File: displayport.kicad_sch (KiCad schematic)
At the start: 56 parts

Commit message: add UART4 connector
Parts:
- C191: renamed from C189; value (none) -> 0.1uF; footprint (none) -> Capacitor_SMD:C_0402_1005Metric
- C194: renamed from C192; value (none) -> 1uF; footprint (none) -> Capacitor_SMD:C_0402_1005Metric
- C200: renamed from C198; value (none) -> 1uF; footprint (none) -> Capacitor_SMD:C_0402_1005Metric
- C206: renamed from C204; value (none) -> 0.1uF; footprint (none) -> qsbc:C_0201_0603Metric
- C207: renamed from C205; value (none) -> 0.1uF; footprint (none) -> qsbc:C_0201_0603Metric
- C208: renamed from C206; value (none) -> 0.1uF; footprint (none) -> qsbc:C_0201_0603Metric
- C209: renamed from C207; value (none) -> 0.1uF; footprint (none) -> qsbc:C_0201_0603Metric
- C210: renamed from C208; value (none) -> 0.1uF; footprint (none) -> qsbc:C_0201_0603Metric
- C211: renamed from C209; value (none) -> 0.1uF; footprint (none) -> qsbc:C_0201_0603Metric
- C212: renamed from C210; value (none) -> 0.1uF; footprint (none) -> qsbc:C_0201_0603Metric
- C213: renamed from C211; value (none) -> 0.1uF; footprint (none) -> qsbc:C_0201_0603Metric
- C214: renamed from C212; value (none) -> 0.1uF; footprint (none) -> qsbc:C_0201_0603Metric
- C215: renamed from C213; value (none) -> 0.1uF; footprint (none) -> qsbc:C_0201_0603Metric
- C218: renamed from C216; value (none) -> 1000pF; footprint (none) -> Capacitor_SMD:C_1210_3225Metric
- R140: renamed from R141; value (none) -> 10K; footprint (none) -> Resistor_SMD:R_0402_1005Metric
- R141: renamed from R142; value (none) -> R; footprint (none) -> Resistor_SMD:R_0402_1005Metric
- R142: renamed from R143; value (none) -> R; footprint (none) -> Resistor_SMD:R_0402_1005Metric
- R145: renamed from R146; value (none) -> 100K; footprint (none) -> Resistor_SMD:R_0402_1005Metric
- R146: renamed from R147; value (none) -> 100K; footprint (none) -> Resistor_SMD:R_0402_1005Metric
- R148: renamed from R149; value (none) -> 1M; footprint (none) -> Resistor_SMD:R_0402_1005Metric
- R150: renamed from R151; value (none) -> 1M; footprint (none) -> Resistor_SMD:R_1206_3216Metric
- U1: value (none) -> MIMX8MM6DVTLZAA; footprint (none) -> qsbc:SOT1967-1
- U35: renamed from U34; value (none) -> LP5912-1.2DRV; footprint (none) -> Package_SON:WSON-6-1EP_2x2mm_P0.65mm_EP1x1.6mm_ThermalVias
- U36: renamed from U35; value (none) -> SN65DSI86; footprint (none) -> qsbc:BGA-64
- U37: renamed from U36; value (none) -> TPD4E02B04; footprint (none) -> Package_SON:USON-10_2.5x1.0mm_P0.5mm
- U38: renamed from U37; value (none) -> TPD4E02B04; footprint (none) -> Package_SON:USON-10_2.5x1.0mm_P0.5mm
- U39: renamed from U38; value (none) -> TPD4E02B04; footprint (none) -> Package_SON:USON-10_2.5x1.0mm_P0.5mm
- U40: renamed from U39; value (none) -> Connector_Displayport_Source; footprint (none) -> qsbc:Connector_Displayport_Molex_472720001
- X1: value (none) -> 26Mhz; footprint (none) -> Oscillator:Oscillator_SMD_ECS_2520MV-xxx-xx-4Pin_2.5x2.0mm
- renumbered C185 to C187, C186 to C188, C187 to C189, C188 to C190, C190 to C192, C191 to C193, C193 to C195, C194 to C196, C195 to C197, C196 to C198, C197 to C199, C199 to C201, C200 to C202, C201 to C203, C202 to C204, C203 to C205, C214 to C216, C215 to C217, R136 to R135, R137 to R136, R138 to R137, R139 to R138, R140 to R139, R144 to R143, R145 to R144, R148 to R147, R150 to R149

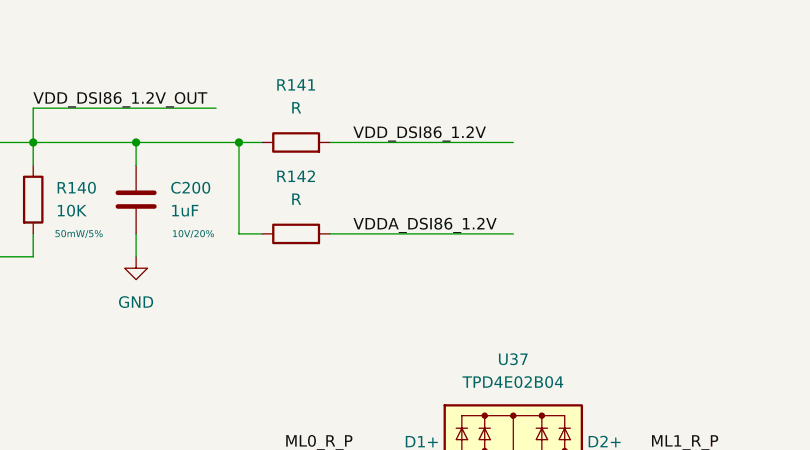
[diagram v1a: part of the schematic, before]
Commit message: change USB-UART conn, add new 0402 fp, more pcb work
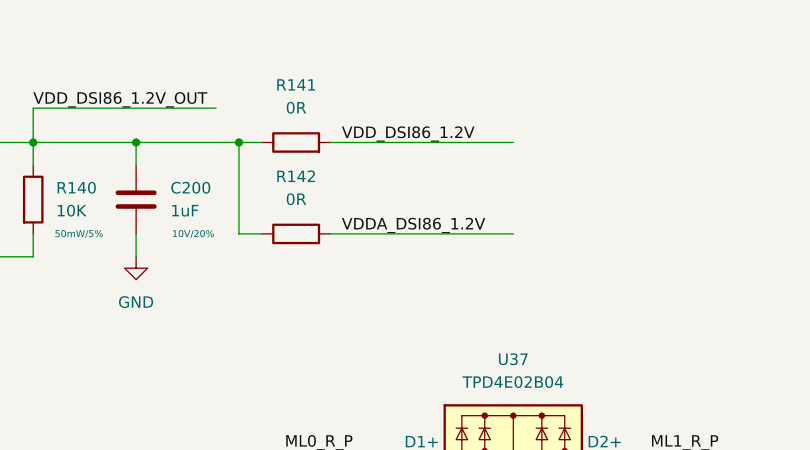
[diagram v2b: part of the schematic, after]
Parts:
- C190, C191, C194, C195, C200, C203: footprint Capacitor_SMD:C_0402_1005Metric -> qsbc:C_0402_1005Metric
- R135, R136, R137, R138, R139, R140, R143, R144, R145, R146, R147, R148, R149: footprint Resistor_SMD:R_0402_1005Metric -> qsbc:R_0402_1005Metric
- R141, R142: value R -> 0R; footprint Resistor_SMD:R_0402_1005Metric -> qsbc:R_0402_1005Metric
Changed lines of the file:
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@@
     (effects (font (size 1.27 1.27)) (justify left bottom))
   )
-  (label "VDDA_DSI86_1.2V" (at 228.6 40.64 0)
+  (label "VDDA_DSI86_1.2V" (at 227.33 40.64 0)
     (effects (font (size 1.27 1.27)) (justify left bottom))
   )
@@
     (effects (font (size 1.27 1.27)) (justify left bottom))
   )
-  (label "VDD_DSI86_1.2V" (at 228.6 30.48 0)
+  (label "VDD_DSI86_1.2V" (at 227.33 30.48 0)
     (effects (font (size 1.27 1.27)) (justify left bottom))
   )
@@
       (effects (font (size 1.27 1.27)) (justify left))
     )
-    (property "Footprint" "Resistor_SMD:R_0402_1005Metric" (id 2) (at 326.898 130.81 90)
+    (property "Footprint" "qsbc:R_0402_1005Metric" (id 2) (at 326.898 130.81 90)
       (effects (font (size 1.27 1.27)) hide)
     )
@@
       (effects (font (size 1.27 1.27)) (justify left))
     )
-    (property "Footprint" "Capacitor_SMD:C_0402_1005Metric" (id 2) (at 242.2652 246.38 0)
+    (property "Footprint" "qsbc:C_0402_1005Metric" (id 2) (at 242.2652 246.38 0)
       (effects (font (size 1.27 1.27)) hide)
     )
@@
     (property "Reference" "R144" (id 0) (at 238.76 147.32 90))
     (property "Value" "51K" (id 1) (at 238.76 149.86 90))
-    (property "Footprint" "Resistor_SMD:R_0402_1005Metric" (id 2) (at 238.76 155.448 90)
+    (property "Footprint" "qsbc:R_0402_1005Metric" (id 2) (at 238.76 155.448 90)
       (effects (font (size 1.27 1.27)) hide)
     )
@@
       (effects (font (size 1.27 1.27)) (justify left))
     )
-    (property "Footprint" "Capacitor_SMD:C_0402_1005Metric" (id 2) (at 205.4352 40.64 0)
+    (property "Footprint" "qsbc:C_0402_1005Metric" (id 2) (at 205.4352 40.64 0)
       (effects (font (size 1.27 1.27)) hide)
     )
@@
       (effects (font (size 1.27 1.27)) (justify left))
     )
-    (property "Footprint" "Resistor_SMD:R_0402_1005Metric" (id 2) (at 115.062 102.87 90)
+    (property "Footprint" "qsbc:R_0402_1005Metric" (id 2) (at 115.062 102.87 90)
       (effects (font (size 1.27 1.27)) hide)
     )
@@
     (property "Reference" "R149" (id 0) (at 359.41 100.33 90))
     (property "Value" "0R" (id 1) (at 359.41 102.87 90))
-    (property "Footprint" "Resistor_SMD:R_0402_1005Metric" (id 2) (at 359.41 108.458 90)
+    (property "Footprint" "qsbc:R_0402_1005Metric" (id 2) (at 359.41 108.458 90)
       (effects (font (size 1.27 1.27)) hide)
     )
@@
       (effects (font (size 1.27 1.27)) (justify left))
     )
-    (property "Footprint" "Resistor_SMD:R_0402_1005Metric" (id 2) (at 347.218 130.81 90)
+    (property "Footprint" "qsbc:R_0402_1005Metric" (id 2) (at 347.218 130.81 90)
       (effects (font (size 1.27 1.27)) hide)
     )
@@
       (effects (font (size 1.27 1.27)) (justify left))
     )
-    (property "Footprint" "Resistor_SMD:R_0402_1005Metric" (id 2) (at 126.492 115.57 90)
+    (property "Footprint" "qsbc:R_0402_1005Metric" (id 2) (at 126.492 115.57 90)
       (effects (font (size 1.27 1.27)) hide)
     )
@@
       (effects (font (size 1.27 1.27)) (justify left))
     )
-    (property "Footprint" "Capacitor_SMD:C_0402_1005Metric" (id 2) (at 111.4552 39.37 0)
+    (property "Footprint" "qsbc:C_0402_1005Metric" (id 2) (at 111.4552 39.37 0)
       (effects (font (size 1.27 1.27)) hide)
     )
@@
     (in_bom yes) (on_board yes) (fields_autoplaced)
     (property "Reference" "R142" (id 0) (at 222.25 34.29 90))
-    (property "Value" "R" (id 1) (at 222.25 36.83 90))
-    (property "Footprint" "Resistor_SMD:R_0402_1005Metric" (id 2) (at 222.25 42.418 90)
+    (property "Value" "0R" (id 1) (at 222.25 36.83 90))
+    (property "Footprint" "qsbc:R_0402_1005Metric" (id 2) (at 222.25 42.418 90)
       (effects (font (size 1.27 1.27)) hide)
     )
@@
       (effects (font (size 1.27 1.27)) (justify left))
     )
-    (property "Footprint" "Resistor_SMD:R_0402_1005Metric" (id 2) (at 126.492 105.41 90)
+    (property "Footprint" "qsbc:R_0402_1005Metric" (id 2) (at 126.492 105.41 90)
       (effects (font (size 1.27 1.27)) hide)
     )
@@
       (effects (font (size 1.27 1.27)) (justify right))
     )
-    (property "Footprint" "Resistor_SMD:R_0402_1005Metric" (id 2) (at 333.502 130.81 90)
+    (property "Footprint" "qsbc:R_0402_1005Metric" (id 2) (at 333.502 130.81 90)
       (effects (font (size 1.27 1.27)) hide)
     )
@@
     (in_bom yes) (on_board yes) (fields_autoplaced)
     (property "Reference" "R141" (id 0) (at 222.25 24.13 90))
-    (property "Value" "R" (id 1) (at 222.25 26.67 90))
-    (property "Footprint" "Resistor_SMD:R_0402_1005Metric" (id 2) (at 222.25 32.258 90)
+    (property "Value" "0R" (id 1) (at 222.25 26.67 90))
+    (property "Footprint" "qsbc:R_0402_1005Metric" (id 2) (at 222.25 32.258 90)
       (effects (font (size 1.27 1.27)) hide)
     )
@@
       (effects (font (size 1.27 1.27)) (justify left))
     )
-    (property "Footprint" "Resistor_SMD:R_0402_1005Metric" (id 2) (at 115.062 92.71 90)
+    (property "Footprint" "qsbc:R_0402_1005Metric" (id 2) (at 115.062 92.71 90)
       (effects (font (size 1.27 1.27)) hide)
     )
@@
       (effects (font (size 1.27 1.27)) (justify left))
     )
-    (property "Footprint" "Resistor_SMD:R_0402_1005Metric" (id 2) (at 335.788 107.95 90)
+    (property "Footprint" "qsbc:R_0402_1005Metric" (id 2) (at 335.788 107.95 90)
       (effects (font (size 1.27 1.27)) hide)
     )
@@
       (effects (font (size 1.27 1.27)) (justify left))
     )
-    (property "Footprint" "Capacitor_SMD:C_0402_1005Metric" (id 2) (at 153.3652 246.38 0)
+    (property "Footprint" "qsbc:C_0402_1005Metric" (id 2) (at 153.3652 246.38 0)
       (effects (font (size 1.27 1.27)) hide)
     )
@@
     (property "Reference" "R139" (id 0) (at 142.24 78.74 90))
     (property "Value" "0R" (id 1) (at 142.24 81.28 90))
-    (property "Footprint" "Resistor_SMD:R_0402_1005Metric" (id 2) (at 142.24 85.598 90)
+    (property "Footprint" "qsbc:R_0402_1005Metric" (id 2) (at 142.24 85.598 90)
       (effects (font (size 1.27 1.27)) hide)
     )
@@
       (effects (font (size 1.27 1.27)) (justify left))
     )
-    (property "Footprint" "Capacitor_SMD:C_0402_1005Metric" (id 2) (at 152.0952 40.64 0)
+    (property "Footprint" "qsbc:C_0402_1005Metric" (id 2) (at 152.0952 40.64 0)
       (effects (font (size 1.27 1.27)) hide)
     )
@@
       (effects (font (size 1.27 1.27)) (justify left))
     )
-    (property "Footprint" "Resistor_SMD:R_0402_1005Metric" (id 2) (at 230.632 173.99 90)
+    (property "Footprint" "qsbc:R_0402_1005Metric" (id 2) (at 230.632 173.99 90)
       (effects (font (size 1.27 1.27)) hide)
     )
@@
       (effects (font (size 1.27 1.27)) (justify left))
     )
-    (property "Footprint" "Capacitor_SMD:C_0402_1005Metric" (id 2) (at 102.5652 246.38 0)
+    (property "Footprint" "qsbc:C_0402_1005Metric" (id 2) (at 102.5652 246.38 0)
       (effects (font (size 1.27 1.27)) hide)
     )
@@
       (effects (font (size 1.27 1.27)) (justify left))
     )
-    (property "Footprint" "Resistor_SMD:R_0402_1005Metric" (id 2) (at 191.262 36.83 90)
-      (effects (font (size 1.27 1.27)) hide)
-    )
+    (property "Footprint" "qsbc:R_0402_1005Metric" (id 2) (at 191.262 36.83 90)
+      (effects (font (size 1.27 1.27)) hide)
+    )

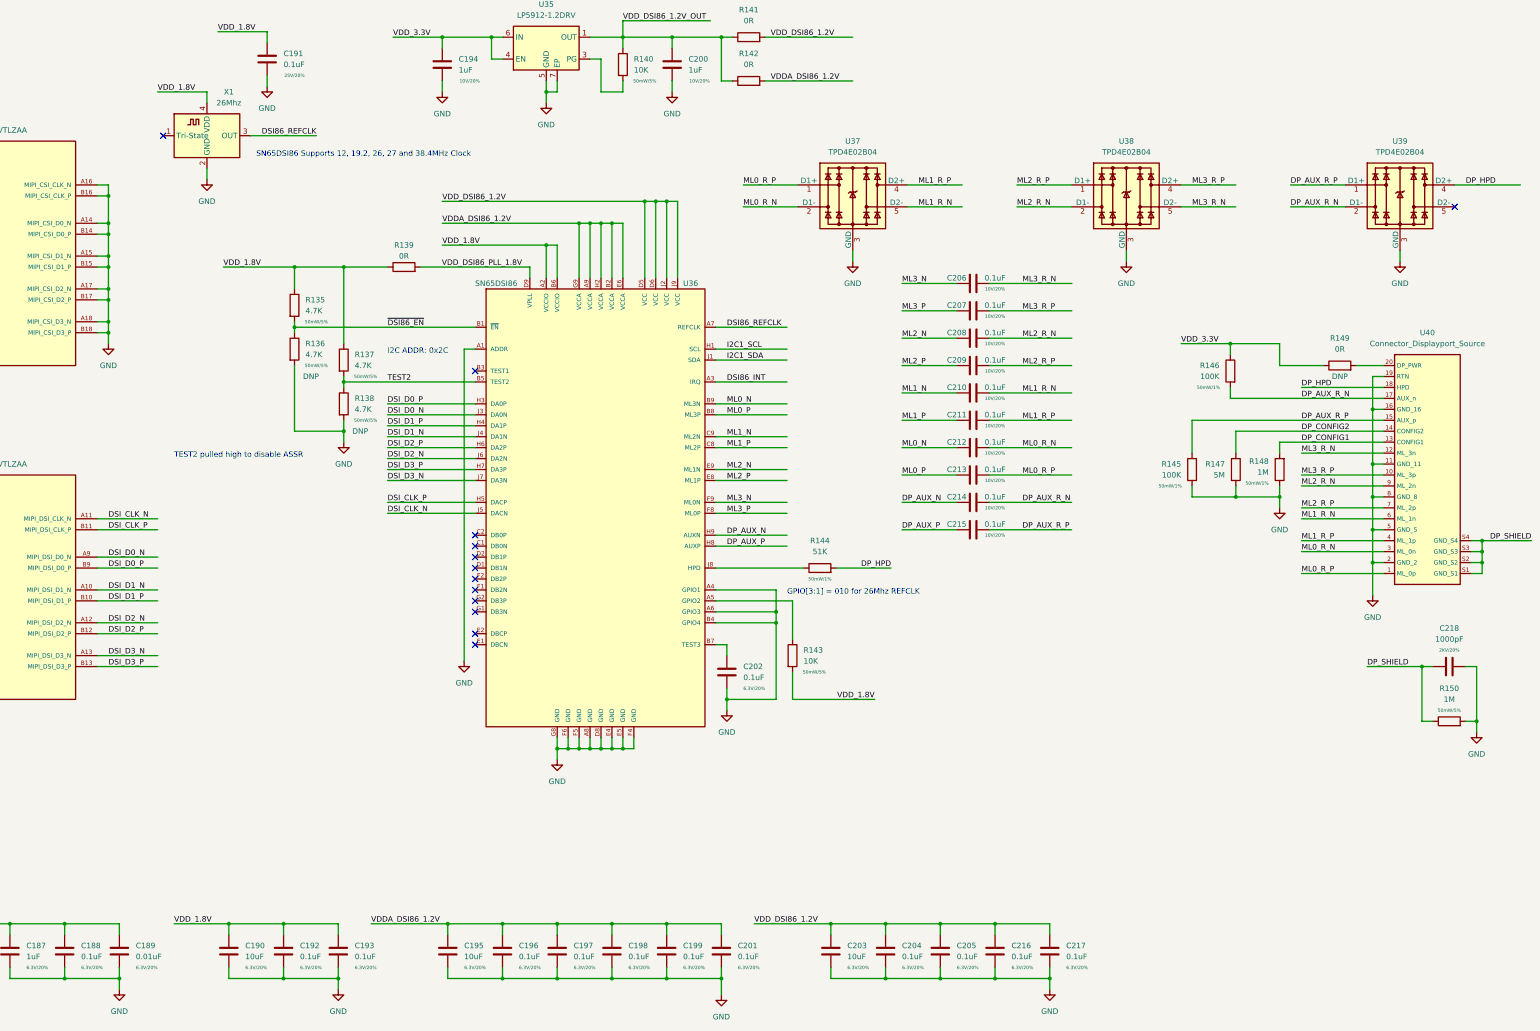
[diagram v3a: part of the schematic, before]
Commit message: bom work, change uart level shifter and m.2 socket
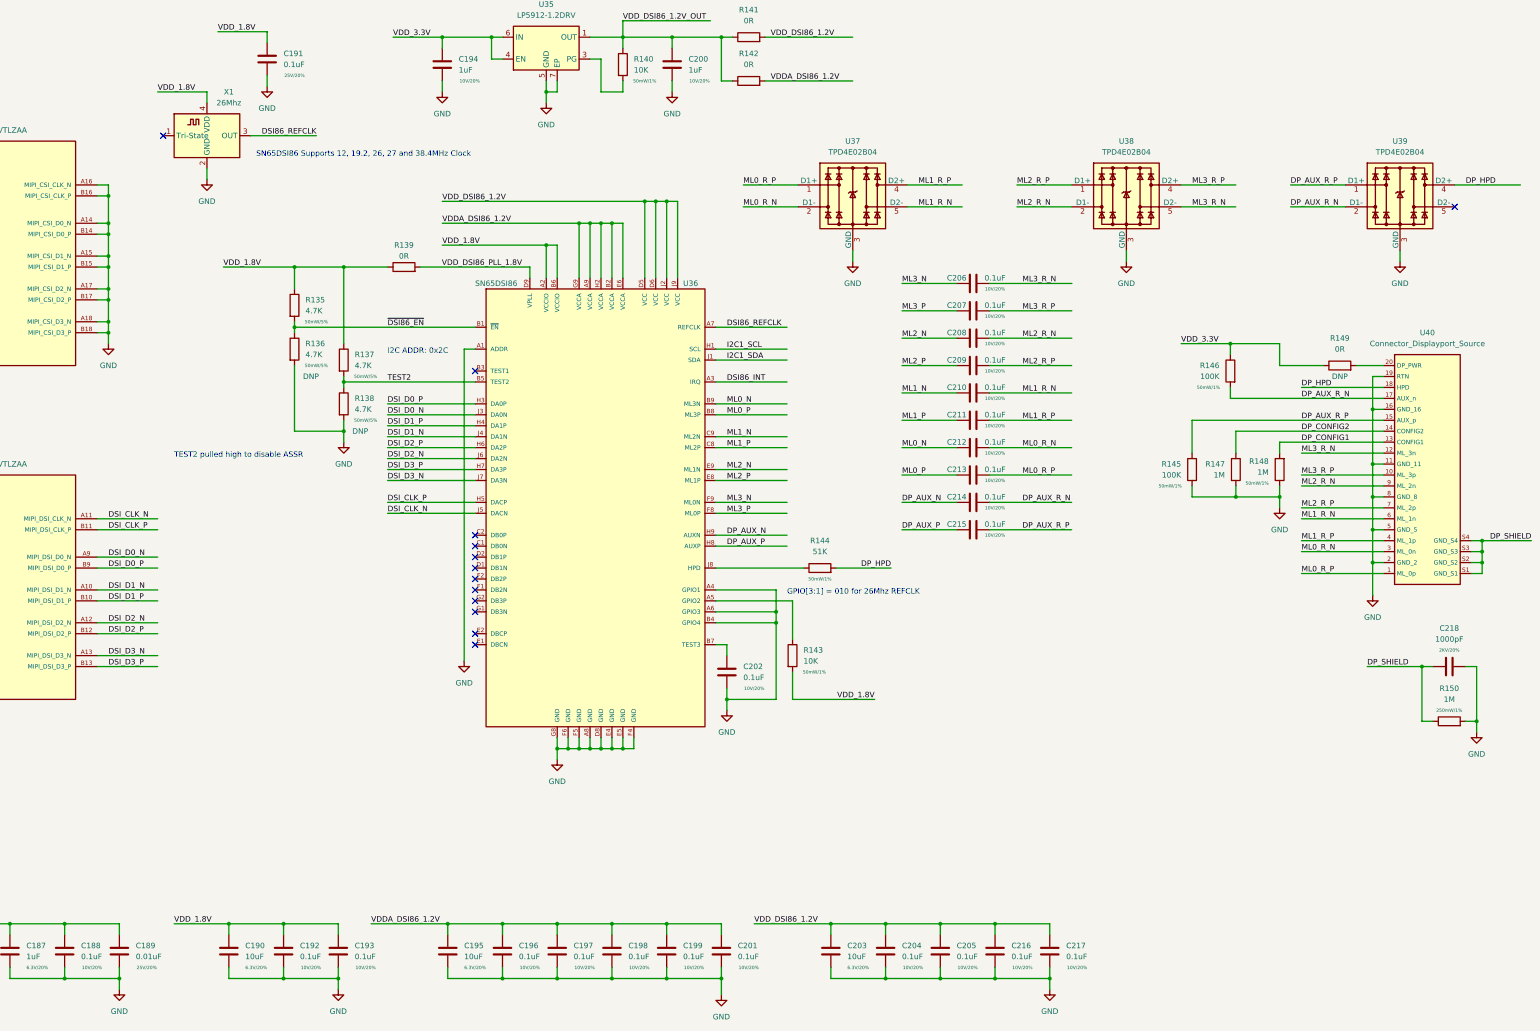
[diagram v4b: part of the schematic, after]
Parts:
- C187: MPN (none) -> GRM033R60J105MEA2D
- C188, C192, C193, C196, C197, C198, C199, C201, C202, C204, C205, C216, C217: MPN (none) -> CL03A104KP3NNNC; Rating 6.3V/20% -> 10V/20%
- C189: MPN (none) -> GRM033R61E103KA12D; Rating 6.3V/20% -> 25V/20%
- C190, C195, C203: MPN (none) -> GRM155R60J106ME44D
- C191: MPN (none) -> CL05A104KA5NNNC
- C194, C200: MPN (none) -> CL05A105KP5NNNC
- C206, C207, C208, C209, C210, C211, C212, C213, C214, C215: MPN (none) -> CL03A104KP3NNNC
- C218: MPN (none) -> C1210C102KGRAC7800
- R135, R136, R137, R138: MPN (none) -> RC0402JR-074K7L
- R139, R141, R142, R149: MPN (none) -> RC0402FR-070RL
- R140, R143: MPN (none) -> RC0402FR-0710KL; Rating 50mW/5% -> 50mW/1%
- R144: MPN (none) -> RC0402FR-0751KL
- R145, R146: MPN (none) -> RC0402FR-07100KL
- R147: value 5M -> 1M; MPN (none) -> RC0402FR-071ML; Rating (none) -> 50mW/1%
- R148: MPN (none) -> RC0402FR-071ML
- R150: MPN (none) -> RC1206FR-071ML; Rating 50mW/5% -> 250mW/1%
- U1: MPN (none) -> MIMX8MM6DVTLZAA
- U35: MPN (none) -> LP5912-1.2DRVR
- U36: MPN (none) -> SN65DSI86ZXHR
- U37, U38, U39: MPN (none) -> TPD4E02B04DQAR
- U40: MPN (none) -> 472720001
